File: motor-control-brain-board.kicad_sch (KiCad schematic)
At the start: 35 parts, among them J1 GPIO, J10 PWM, J11 PWR, J12 POWER_SENSE, J13 MISC_SENSE, J2 I2C, J3 SERIAL_1, J4 SERIAL_2, J5 CAN, J6 SPI, J7 USB_C_Receptacle_USB2.0_16P, J8 SWD, J9 POS_SENSE, SW1 RST, U1 TLV76750QWDRBxQ1, U2 TLV76733QWDRBxQ1

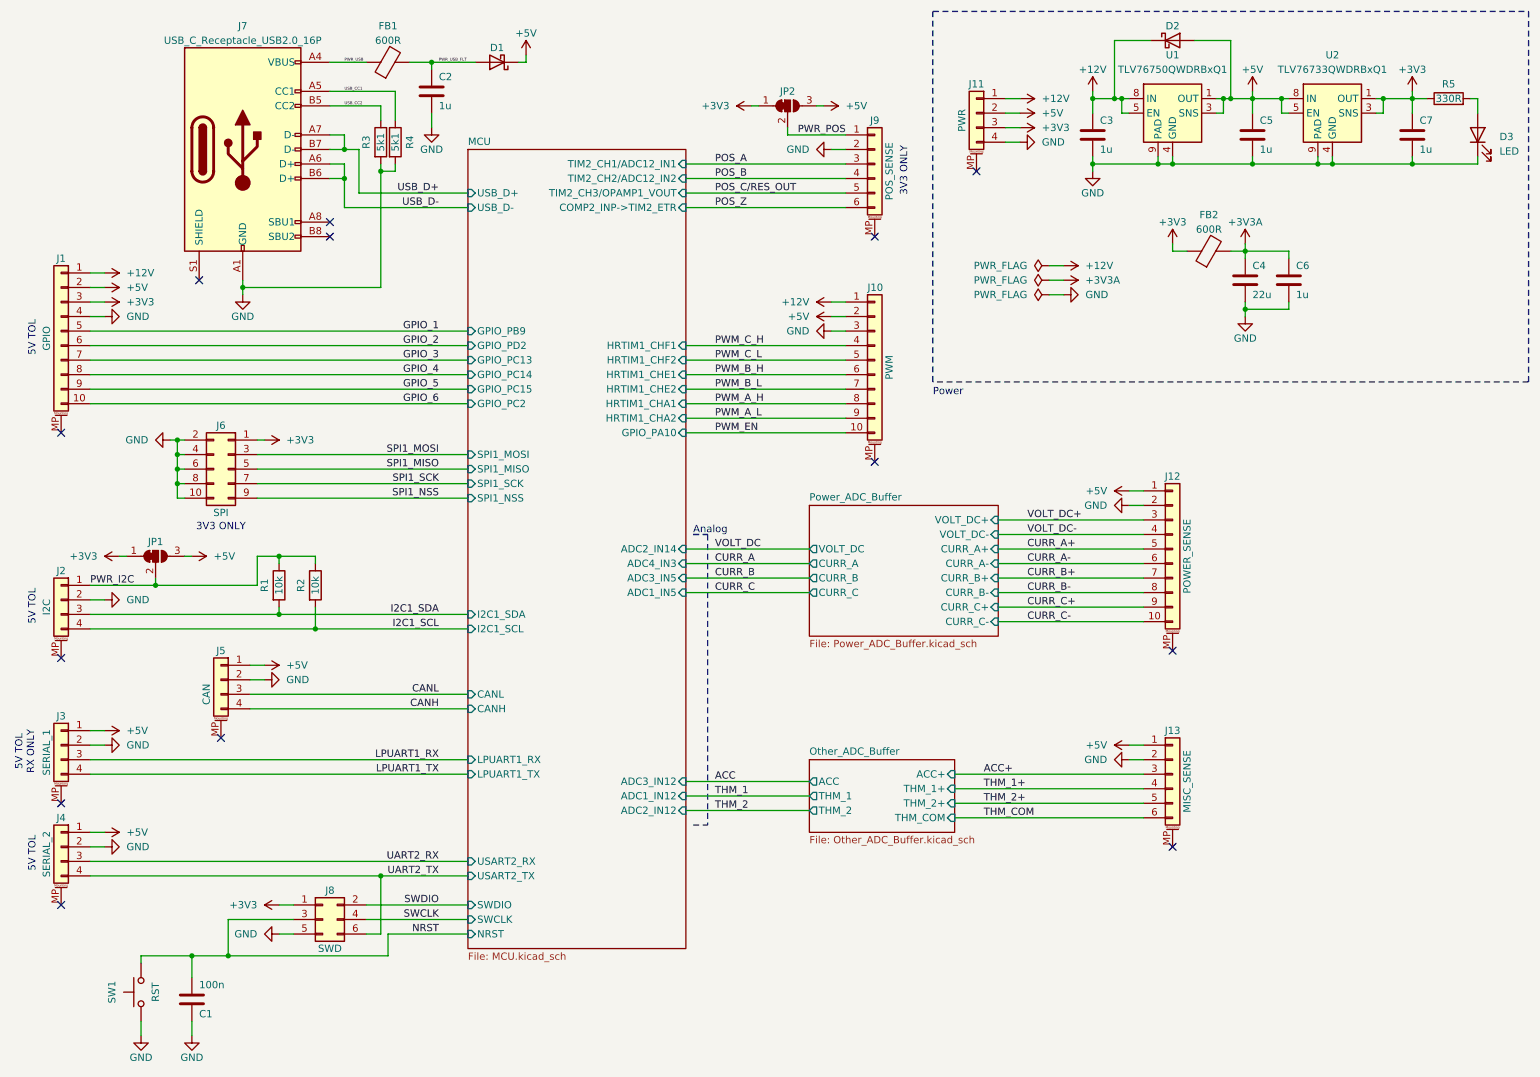
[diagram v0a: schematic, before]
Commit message: Updating all decoupling to 1u
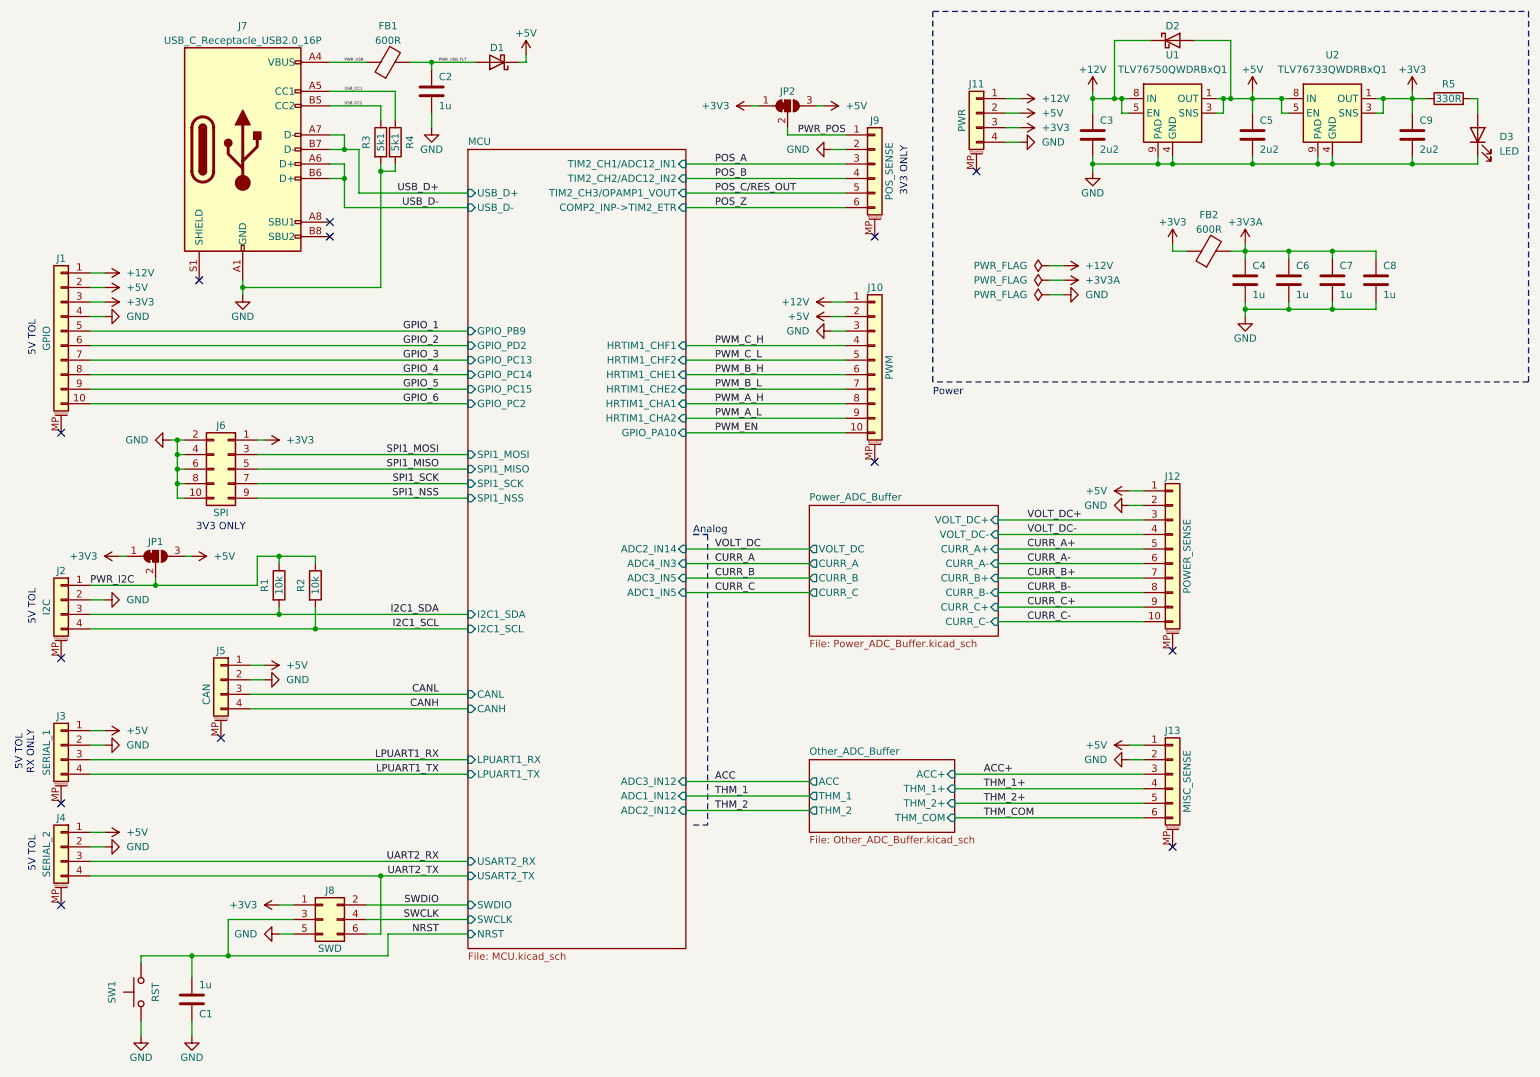
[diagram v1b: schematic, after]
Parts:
- added C7, C8: 1u, Capacitor_SMD:C_0402_1005Metric, symbol Device:C
- C1: value 100n -> 1u
- C2, C6: footprint Capacitor_SMD:C_0603_1608Metric -> Capacitor_SMD:C_0402_1005Metric
- C3, C5: value 1u -> 2u2
- C4: value 22u -> 1u; footprint Capacitor_SMD:C_0805_2012Metric -> Capacitor_SMD:C_0402_1005Metric
- C9: renamed from C7; value 1u -> 2u2
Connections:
- net +3V3A: now also C7.1, C8.1
- net GND: now also C7.2, C8.2
